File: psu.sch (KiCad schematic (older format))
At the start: 35 parts, among them U10 TPS61041DBV, U2 LM5017MR, U3 TPS76333

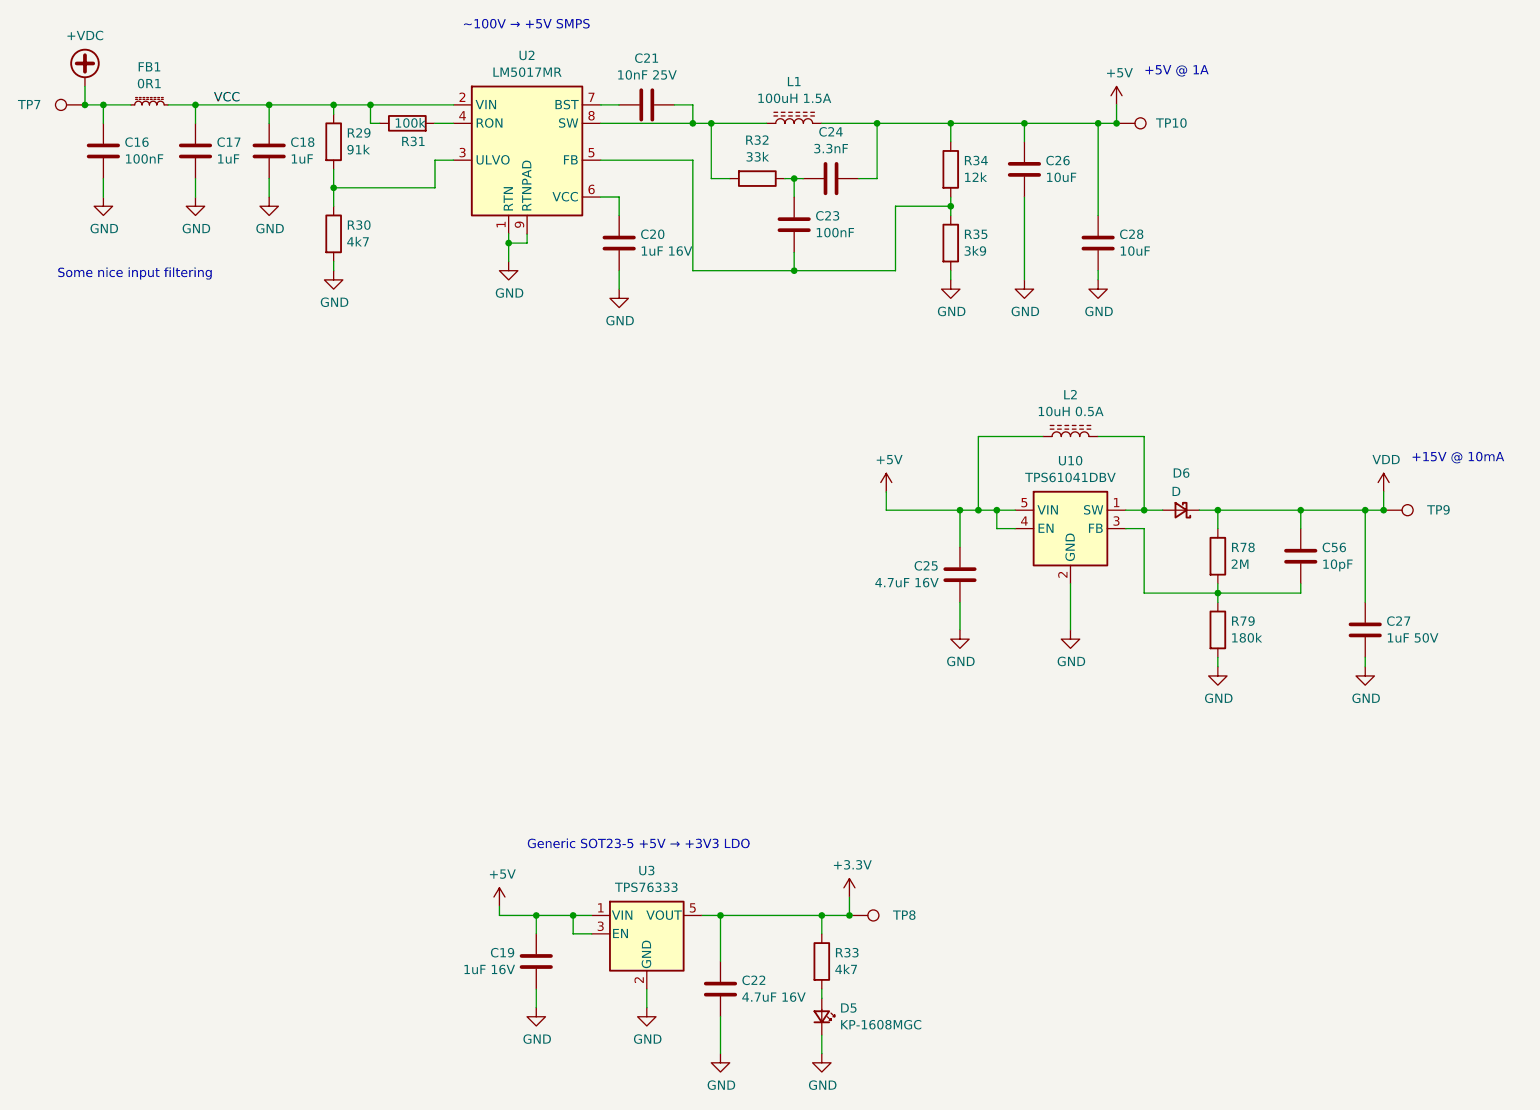
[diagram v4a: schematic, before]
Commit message: Updated part numbers
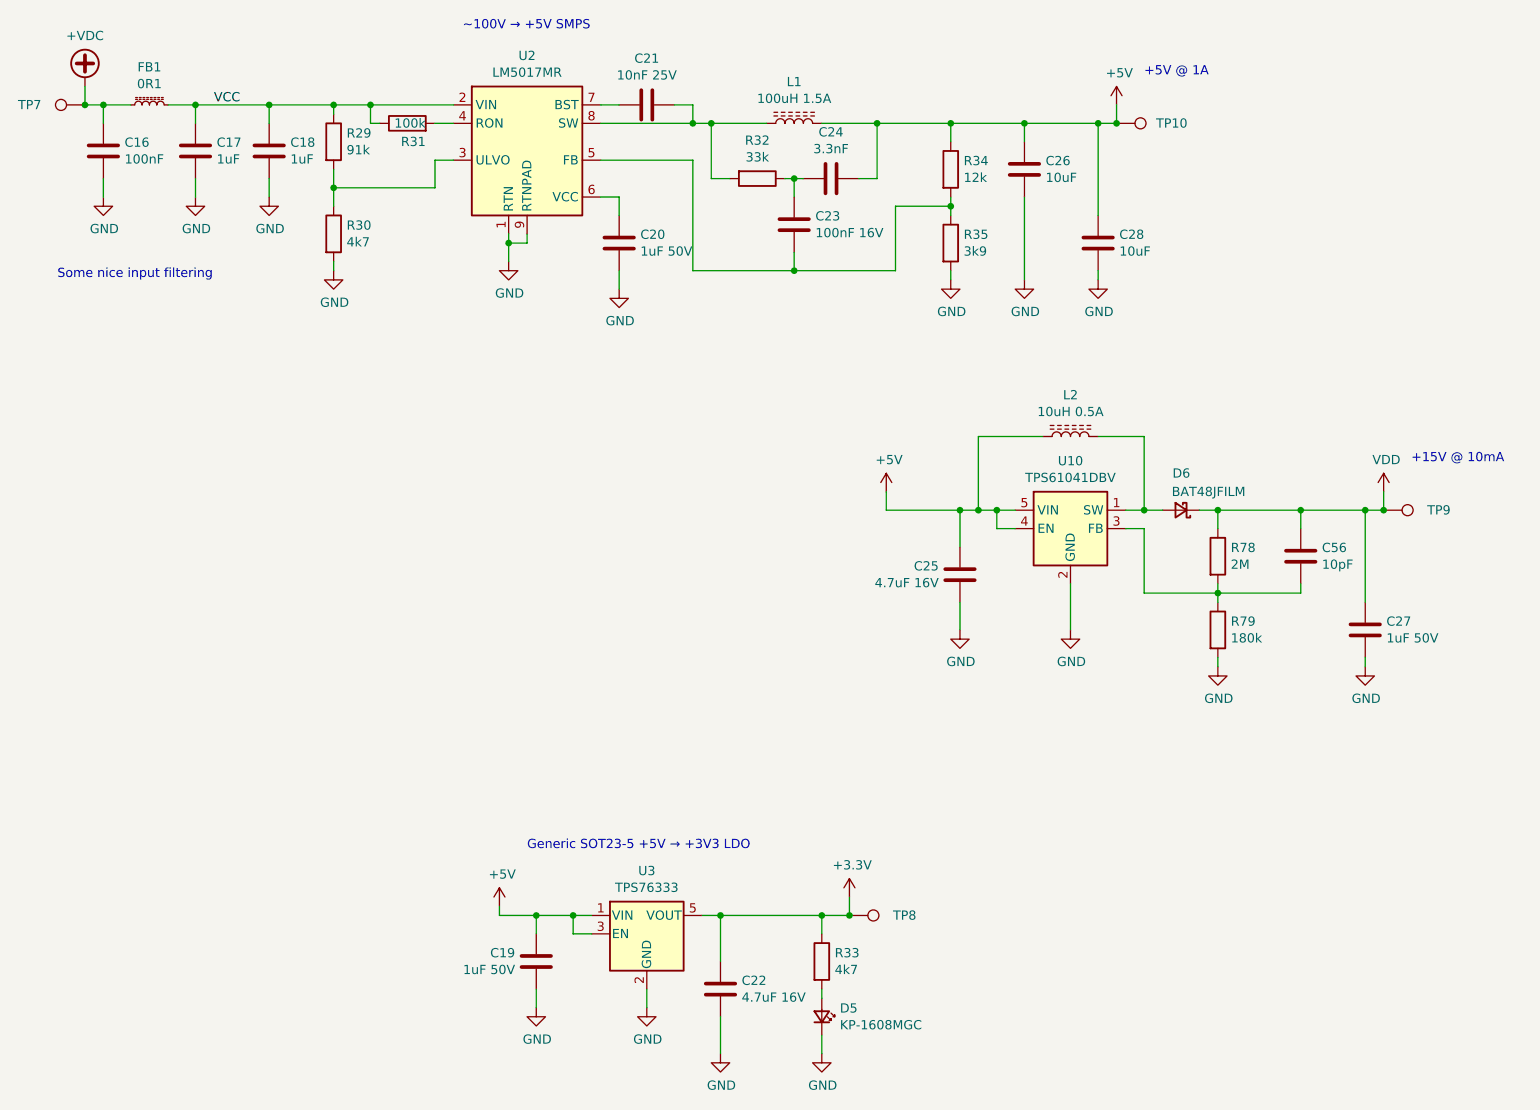
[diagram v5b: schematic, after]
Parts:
- C16, C17, C18, C21, C22, C24, C25, C26, C27, C28, C56, FB1, L1, L2, R32, R33, R34, R35, R78, R79, TP10, TP7, TP8, TP9, U10, U2: Checked (none) -> Yes
- C19, C20: value 1uF 16V -> 1uF 50V; Checked (none) -> Yes
- C23: value 100nF -> 100nF 16V; Checked (none) -> Yes
- D5: Checked (none) -> Yes; LCSC (none) -> C192316
- D6: value D -> BAT48JFILM; Checked (none) -> Yes; LCSC (none) -> C109204
- R29: Checked (none) -> Yes; LCSC (none) -> C23265
- R30: Checked (none) -> Yes; LCSC (none) -> C23162
- R31: Checked (none) -> Yes; LCSC (none) -> C25803
- U3: Checked (none) -> Yes; LCSC C160916 -> C296219
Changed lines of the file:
@@
 F 3 "http://www.ti.com/lit/ds/symlink/lm5017.pdf" H 3800 1700 50  0001 C CNN
 F 4 "C34355" H 3800 1700 50  0001 C CNN "LCSC"
+F 5 "Yes" H 3800 1700 50  0001 C CNN "Checked"
 	1    3800 1700
 	1    0    0    -1
@@
 F 2 "Resistor_SMD:R_0603_1608Metric" V 2680 1700 50  0001 C CNN
 F 3 "~" H 2750 1700 50  0001 C CNN
-F 4 "" H 2750 1700 50  0001 C CNN "LCSC"
+F 4 "C23265" H 2750 1700 50  0001 C CNN "LCSC"
+F 5 "Yes" H 2750 1700 50  0001 C CNN "Checked"
 	1    2750 1700
 	1    0    0    -1
@@
 F 2 "Resistor_SMD:R_0603_1608Metric" V 2680 2200 50  0001 C CNN
 F 3 "~" H 2750 2200 50  0001 C CNN
-F 4 "" H 2750 2200 50  0001 C CNN "LCSC"
+F 4 "C23162" H 2750 2200 50  0001 C CNN "LCSC"
+F 5 "Yes" H 2750 2200 50  0001 C CNN "Checked"
 	1    2750 2200
 	1    0    0    -1
@@
 P 3850 6150
 F 0 "C19" H 3965 6196 50  0000 L CNN
-F 1 "1uF 16V" H 3965 6105 50  0000 L CNN
+F 1 "1uF 50V" H 3965 6105 50  0000 L CNN
 F 2 "Capacitor_SMD:C_0603_1608Metric" H 3888 6000 50  0001 C CNN
 F 3 "~" H 3850 6150 50  0001 C CNN
 F 4 "C15849" H 3850 6150 50  0001 C CNN "LCSC"
+F 5 "Yes" H 3850 6150 50  0001 C CNN "Checked"
 	1    3850 6150
 	-1   0    0    -1
@@
 F 3 "~" H 4850 6300 50  0001 C CNN
 F 4 "C19666" H 4850 6300 50  0001 C CNN "LCSC"
+F 5 "Yes" H 4850 6300 50  0001 C CNN "Checked"
 	1    4850 6300
 	-1   0    0    -1
@@
 F 2 "Package_TO_SOT_SMD:SOT-23-5" H 4450 6325 50  0001 C CIN
 F 3 "http://www.ti.com/lit/ds/symlink/tps763.pdf" H 4450 6000 50  0001 C CNN
-F 4 "C160916" H 4450 6000 50  0001 C CNN "LCSC"
+F 4 "C296219" H 4450 6000 50  0001 C CNN "LCSC"
+F 5 "Yes" H 4450 6000 50  0001 C CNN "Checked"
 	1    4450 6000
 	1    0    0    -1
@@
 F 3 "~" H 4450 1500 50  0001 C CNN
 F 4 "C57112" H 4450 1500 50  0001 C CNN "LCSC"
+F 5 "Yes" H 4450 1500 50  0001 C CNN "Checked"
 	1    4450 1500
 	0    1    1    0
@@
 P 4300 2250
 F 0 "C20" H 4415 2296 50  0000 L CNN
-F 1 "1uF 16V" H 4415 2205 50  0000 L CNN
+F 1 "1uF 50V" H 4415 2205 50  0000 L CNN
 F 2 "Capacitor_SMD:C_0603_1608Metric" H 4338 2100 50  0001 C CNN
 F 3 "~" H 4300 2250 50  0001 C CNN
 F 4 "C15849" H 4300 2250 50  0001 C CNN "LCSC"
+F 5 "Yes" H 4300 2250 50  0001 C CNN "Checked"
 	1    4300 2250
 	1    0    0    -1
@@
 F 3 "~" H 6100 1850 50  0001 C CNN
 F 4 "C25752" H 6100 1850 50  0001 C CNN "LCSC"
+F 5 "Yes" H 6100 1850 50  0001 C CNN "Checked"
 	1    6100 1850
 	1    0    0    -1
@@
 F 3 "~" H 6100 2250 50  0001 C CNN
 F 4 "C51721" H 6100 2250 50  0001 C CNN "LCSC"
+F 5 "Yes" H 6100 2250 50  0001 C CNN "Checked"
 	1    6100 2250
 	1    0    0    -1
@@
 F 3 "~" H 6900 2250 50  0001 C CNN
 F 4 "C13585" H 6900 2250 50  0001 C CNN "LCSC"
+F 5 "Yes" H 6900 2250 50  0001 C CNN "Checked"
 	1    6900 2250
 	1    0    0    -1
@@
 F 3 "~" H 1500 1750 50  0001 C CNN
 F 4 "C28233" H 1500 1750 50  0001 C CNN "LCSC"
+F 5 "Yes" H 1500 1750 50  0001 C CNN "Checked"
 	1    1500 1750
 	1    0    0    -1
@@
 F 3 "~" H 2000 1750 50  0001 C CNN
 F 4 "C13832" H 2000 1750 50  0001 C CNN "LCSC"
+F 5 "Yes" H 2000 1750 50  0001 C CNN "Checked"
 	1    2000 1750
 	1    0    0    -1
@@
 F 3 "~" H 2400 1750 50  0001 C CNN
 F 4 "C13832" H 2400 1750 50  0001 C CNN "LCSC"
+F 5 "Yes" H 2400 1750 50  0001 C CNN "Checked"
 	1    2400 1750
 	1    0    0    -1
@@
 F 3 "~" H 5450 1900 50  0001 C CNN
 F 4 "C26404" H 5450 1900 50  0001 C CNN "LCSC"
+F 5 "Yes" H 5450 1900 50  0001 C CNN "Checked"
 	1    5450 1900
 	0    1    1    0
@@
 F 3 "~" H 5050 1900 50  0001 C CNN
 F 4 "C25779" H 5050 1900 50  0001 C CNN "LCSC"
+F 5 "Yes" H 5050 1900 50  0001 C CNN "Checked"
 	1    5050 1900
 	0    1    1    0
@@
 P 5250 2150
 F 0 "C23" H 5365 2196 50  0000 L CNN
-F 1 "100nF" H 5365 2105 50  0000 L CNN
+F 1 "100nF 16V" H 5365 2105 50  0000 L CNN
 F 2 "Capacitor_SMD:C_0402_1005Metric" H 5288 2000 50  0001 C CNN
 F 3 "~" H 5250 2150 50  0001 C CNN
 F 4 "C1525" H 5250 2150 50  0001 C CNN "LCSC"
+F 5 "Yes" H 5250 2150 50  0001 C CNN "Checked"
 	1    5250 2150
 	1    0    0    -1
@@
 F 3 "~" H 6150 4050 50  0001 C CNN
 F 4 "C19666" H 6150 4050 50  0001 C CNN "LCSC"
+F 5 "Yes" H 6150 4050 50  0001 C CNN "Checked"
 	1    6150 4050
 	-1   0    0    -1
@@
 F 2 "Resistor_SMD:R_0603_1608Metric" V 3080 1600 50  0001 C CNN
 F 3 "~" H 3150 1600 50  0001 C CNN
-F 4 "" H 3150 1600 50  0001 C CNN "LCSC"
+F 4 "C25803" H 3150 1600 50  0001 C CNN "LCSC"
+F 5 "Yes" H 3150 1600 50  0001 C CNN "Checked"
 	1    3150 1600
 	0    -1   -1   0
@@
 F 3 "~" H 8350 4350 50  0001 C CNN
 F 4 "C15849" H 8350 4350 50  0001 C CNN "LCSC"
+F 5 "Yes" H 8350 4350 50  0001 C CNN "Checked"
 	1    8350 4350
 	1    0    0    -1
@@
 F 3 "~" H 6500 1850 50  0001 C CNN
 F 4 "C13585" H 6500 1850 50  0001 C CNN "LCSC"
+F 5 "Yes" H 6500 1850 50  0001 C CNN "Checked"
 	1    6500 1850
 	1    0    0    -1
@@
 F 3 "~" H 8650 3700 50  0001 C CNN
 F 4 "~" H 8450 3700 50  0001 C CNN "LCSC"
+F 5 "Yes" H 8450 3700 50  0001 C CNN "Checked"
 	1    8450 3700
 	0    1    -1   0
@@
 F 3 "~" H 7200 1600 50  0001 C CNN
 F 4 "~" H 7000 1600 50  0001 C CNN "LCSC"
+F 5 "Yes" H 7000 1600 50  0001 C CNN "Checked"
 	1    7000 1600
 	0    1    -1   0
@@
 F 3 "~" H 1600 1500 50  0001 C CNN
 F 4 "~" H 1400 1500 50  0001 C CNN "LCSC"
+F 5 "Yes" H 1400 1500 50  0001 C CNN "Checked"
 	1    1400 1500
 	0    -1   -1   0
@@
 F 3 "~" H 5750 5900 50  0001 C CNN
 F 4 "~" H 5550 5900 50  0001 C CNN "LCSC"
+F 5 "Yes" H 5550 5900 50  0001 C CNN "Checked"
 	1    5550 5900
 	0    1    -1   0
@@
 F 2 "Diode_SMD:D_0603_1608Metric" V 5400 6450 50  0001 C CNN
 F 3 "~" V 5400 6450 50  0001 C CNN
+F 4 "C192316" H 5400 6450 50  0001 C CNN "LCSC"
+F 5 "Yes" H 5400 6450 50  0001 C CNN "Checked"
 	1    5400 6450
 	0    1    -1   0
@@
 F 3 "~" H 5400 6150 50  0001 C CNN
 F 4 "C25900" H 5400 6150 50  0001 C CNN "LCSC"
+F 5 "Yes" H 5400 6150 50  0001 C CNN "Checked"
 	1    5400 6150
 	1    0    0    -1
@@
 F 3 "~" H 5250 1600 50  0001 C CNN
 F 4 "C497890" V 5250 1600 50  0001 C CNN "LCSC"
+F 5 "Yes" H 5250 1600 50  0001 C CNN "Checked"
 	1    5250 1600
 	0    -1   -1   0
@@
 F 3 "http://www.ti.com/lit/ds/symlink/tps61040.pdf" H 6550 4100 50  0001 C CNN
 F 4 "C9846" H 6750 3800 50  0001 C CNN "LCSC"
+F 5 "Yes" H 6750 3800 50  0001 C CNN "Checked"
 	1    6750 3800
 	1    0    0    -1
@@
 F 3 "~" H 6750 3300 50  0001 C CNN
 F 4 "C281113" V 6750 3300 50  0001 C CNN "LCSC"
+F 5 "Yes" H 6750 3300 50  0001 C CNN "Checked"
 	1    6750 3300
 	0    -1   -1   0
@@
 F 3 "~" H 7550 4350 50  0001 C CNN
 F 4 "C25760" H 7550 4350 50  0001 C CNN "LCSC"
+F 5 "Yes" H 7550 4350 50  0001 C CNN "Checked"
 	1    7550 4350
 	1    0    0    -1
@@
 F 3 "~" H 8000 3950 50  0001 C CNN
 F 4 "C32949" H 8000 3950 50  0001 C CNN "LCSC"
+F 5 "Yes" H 8000 3950 50  0001 C CNN "Checked"
 	1    8000 3950
 	1    0    0    -1
@@
 AR Path="/6071142D/6099E46D" Ref="D6"  Part="1"
 F 0 "D6" H 7300 3500 50  0000 L CNN
-F 1 "D" H 7350 3600 50  0000 L CNN
+F 1 "BAT48JFILM" H 7000 3600 50  0000 L CNN
 F 2 "Diode_SMD:D_SOD-323" V 7350 3700 50  0001 C CNN
 F 3 "~" V 7350 3700 50  0001 C CNN
+F 4 "Yes" H 7350 3700 50  0001 C CNN "Checked"
+F 5 "C109204" H 7350 3700 50  0001 C CNN "LCSC"
 	1    7350 3700
 	-1   0    0    1
@@
 F 3 "~" H 7550 3950 50  0001 C CNN
 F 4 "C11512" H 7550 3950 50  0001 C CNN "LCSC"
+F 5 "Yes" H 7550 3950 50  0001 C CNN "Checked"
 	1    7550 3950
 	1    0    0    -1
@@
 F 3 "~" H 1750 1500 50  0001 C CNN
 F 4 "C80165" V 1750 1500 50  0001 C CNN "LCSC"
+F 5 "Yes" H 1750 1500 50  0001 C CNN "Checked"
 	1    1750 1500
 	0    -1   -1   0

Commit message: upgrading to 4layer
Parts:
- TP10, TP7, TP8, TP9: footprint TestPoint:TestPoint_Pad_D1.5mm -> TestPoint:TestPoint_Pad_D1.0mm
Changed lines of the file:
@@
 F 0 "TP9" V 8450 4000 50  0000 C CNN
 F 1 "TestPoint" V 8554 3772 50  0001 C CNN
-F 2 "TestPoint:TestPoint_Pad_D1.5mm" H 8650 3700 50  0001 C CNN
+F 2 "TestPoint:TestPoint_Pad_D1.0mm" H 8650 3700 50  0001 C CNN
 F 3 "~" H 8650 3700 50  0001 C CNN
 F 4 "~" H 8450 3700 50  0001 C CNN "LCSC"
@@
 F 0 "TP10" V 7000 1900 50  0000 C CNN
 F 1 "TestPoint" V 7104 1672 50  0001 C CNN
-F 2 "TestPoint:TestPoint_Pad_D1.5mm" H 7200 1600 50  0001 C CNN
+F 2 "TestPoint:TestPoint_Pad_D1.0mm" H 7200 1600 50  0001 C CNN
 F 3 "~" H 7200 1600 50  0001 C CNN
 F 4 "~" H 7000 1600 50  0001 C CNN "LCSC"
@@
 F 0 "TP7" V 1400 1800 50  0000 C CNN
 F 1 "TestPoint" V 1504 1572 50  0001 C CNN
-F 2 "TestPoint:TestPoint_Pad_D1.5mm" H 1600 1500 50  0001 C CNN
+F 2 "TestPoint:TestPoint_Pad_D1.0mm" H 1600 1500 50  0001 C CNN
 F 3 "~" H 1600 1500 50  0001 C CNN
 F 4 "~" H 1400 1500 50  0001 C CNN "LCSC"
@@
 F 0 "TP8" V 5550 6200 50  0000 C CNN
 F 1 "TestPoint" V 5654 5972 50  0001 C CNN
-F 2 "TestPoint:TestPoint_Pad_D1.5mm" H 5750 5900 50  0001 C CNN
+F 2 "TestPoint:TestPoint_Pad_D1.0mm" H 5750 5900 50  0001 C CNN
 F 3 "~" H 5750 5900 50  0001 C CNN
 F 4 "~" H 5550 5900 50  0001 C CNN "LCSC"
